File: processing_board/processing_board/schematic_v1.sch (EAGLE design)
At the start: 64 parts, among them J5 FEMALE 2x3, Q1 BSS138, Q2 BSS138, Q3 BSS138, Q4 BSS138

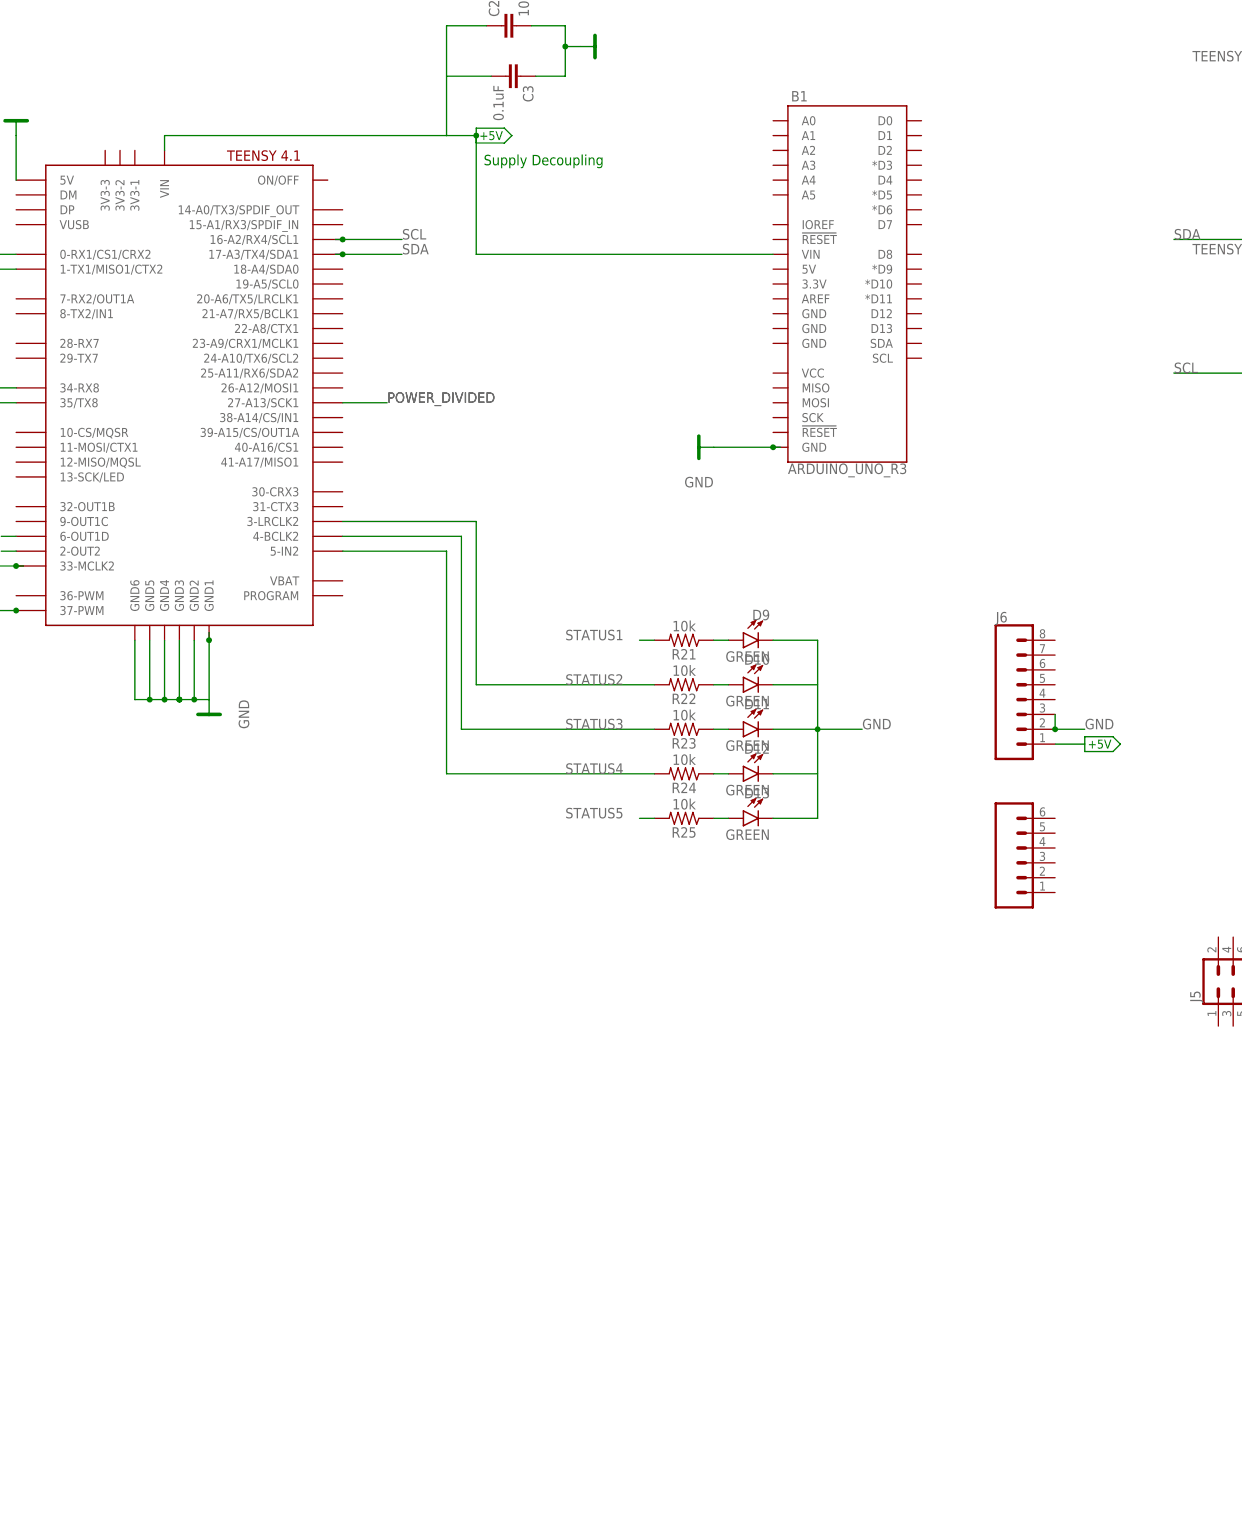
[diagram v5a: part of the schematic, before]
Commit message: added dip switch
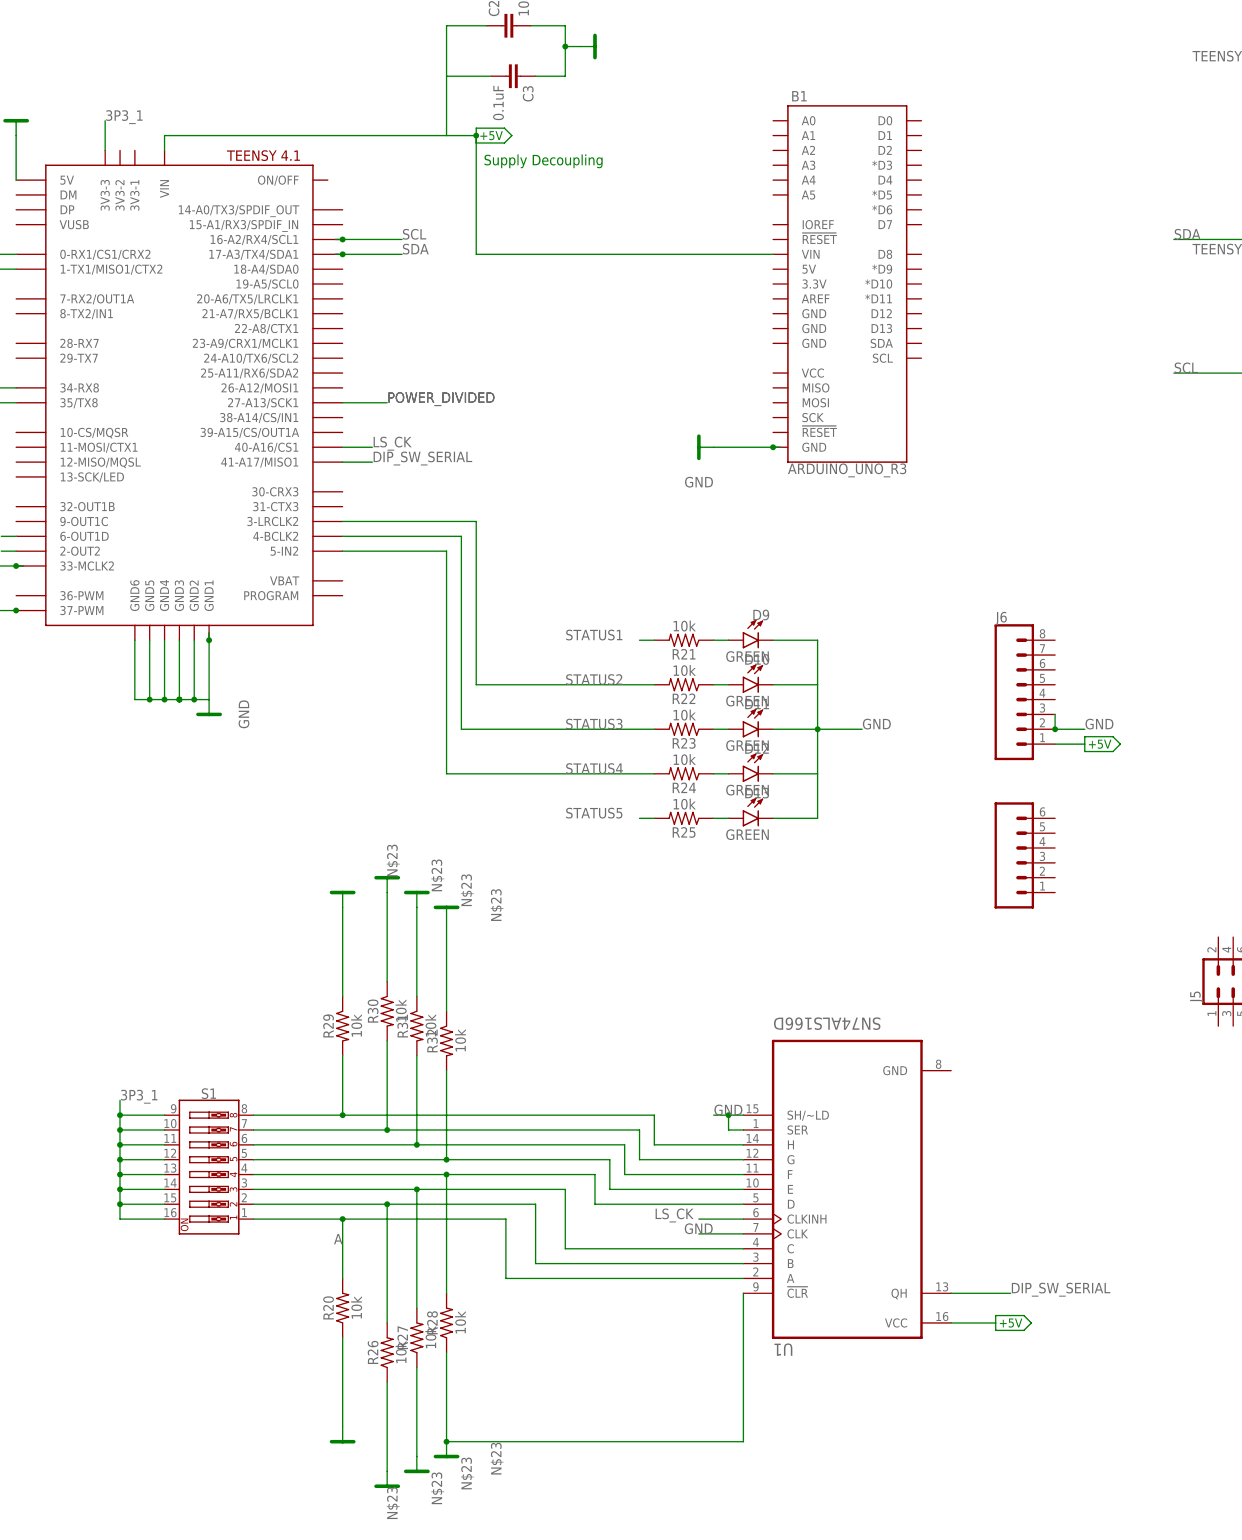
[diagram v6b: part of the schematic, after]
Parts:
- added R20, R26, R27, R28, R29, R30, R31, R32: 10k, SparkFun-Resistors:10KOHM-0603-1/10W-1%
- added S1: (no value), SparkFun-Switches:DIP-08-PTH
- added U1: SN74ALS166D, SN74ALS166D - TI level shifter:SN74ALS166D
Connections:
- new net 3P3_1: S1.10, S1.11, S1.12, S1.13, S1.14, S1.15, S1.16, S1.9, U$4.3V3-3
- new net A: R20.2, S1.1, U1.A
- new net C: R27.2, S1.3, U1.C
- new net D: R28.2, S1.4, U1.D
- new net DIP_SW_SERIAL: U$4.41-A17/MISO1, U1.QH
- new net E: R32.2, S1.5, U1.E
- new net H: R29.2, S1.8, U1.H
- new net LS_CK: U$4.40-A16/CS1, U1.CLKINH
- new net N$23: R20.1, R26.1, R27.1, R28.1, R29.1, R30.1, R31.1, R32.1, U1.!CLR
- new net N$25: R31.2, S1.6, U1.F
- new net N$30: R26.2, S1.2, U1.B
- new net N$9: R30.2, S1.7, U1.G
- net +5V: now also U1.VCC
- net GND: now also U1.CLK, U1.SER, U1.SH/~LD

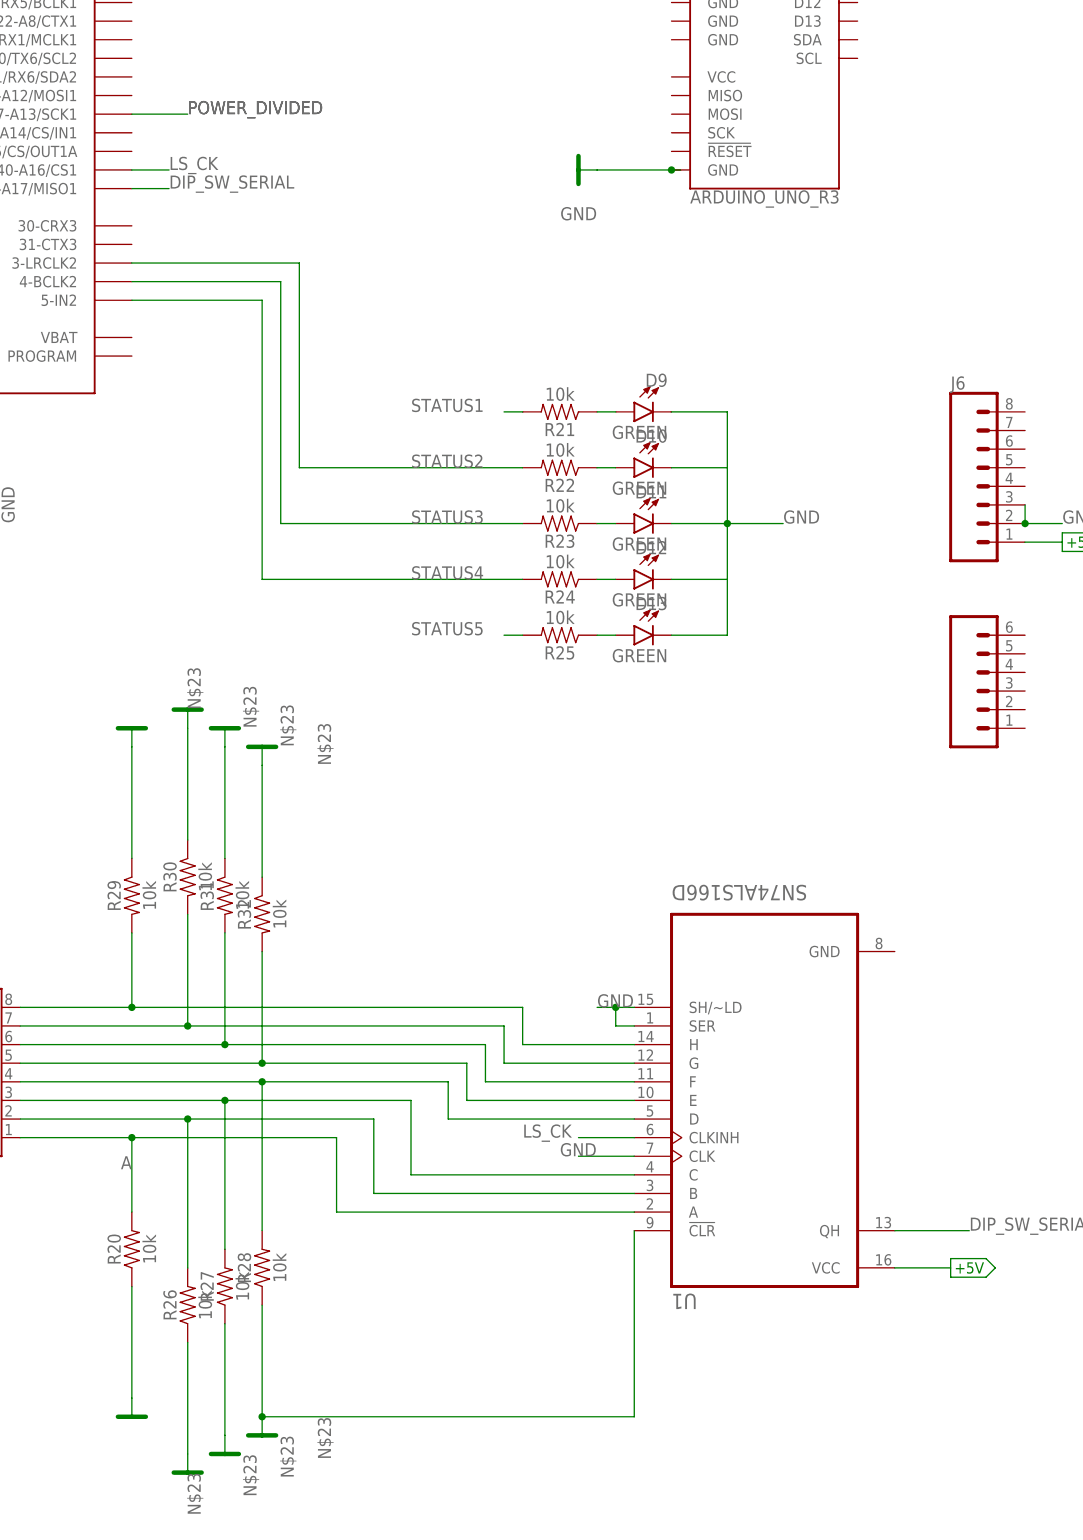
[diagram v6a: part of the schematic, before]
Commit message: fixed dip sw
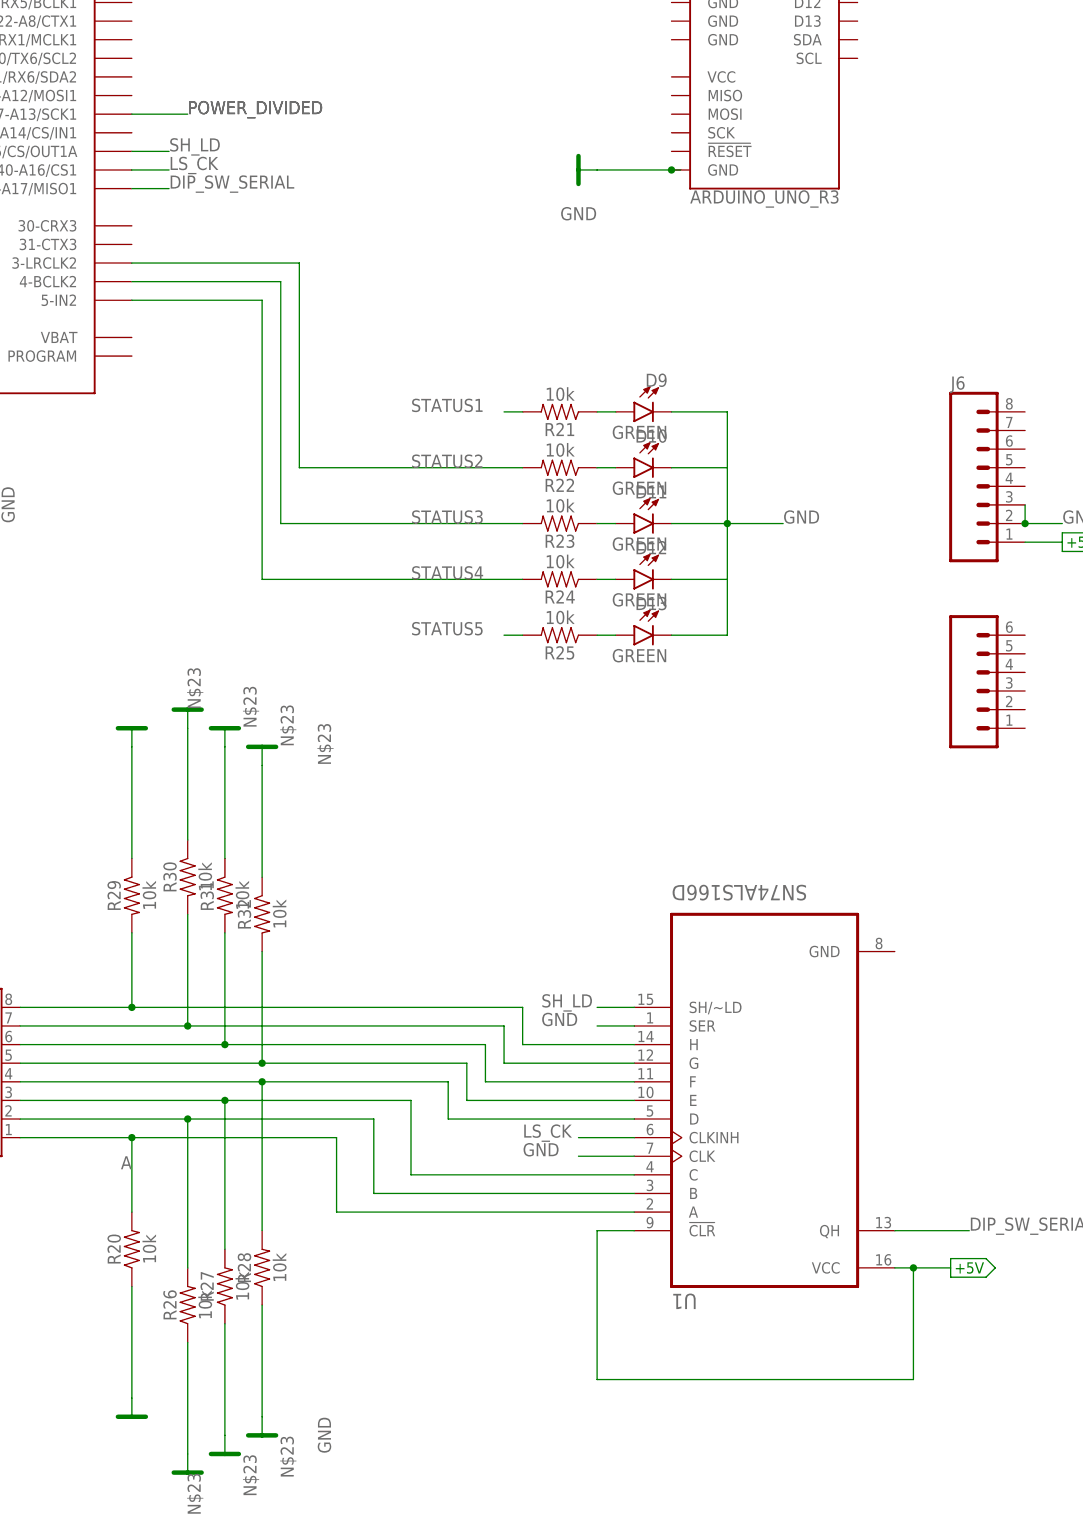
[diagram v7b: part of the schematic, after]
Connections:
- new net SH_LD: U$4.39-A15/CS/OUT1A, U1.SH/~LD
- net +5V: now also U1.!CLR
- net GND: now also R28.1; no longer U1.SH/~LD
- net N$23: no longer R28.1, U1.!CLR
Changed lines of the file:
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@@
 </segment>
 <segment>
-<pinref part="U1" gate="A" pin="SH/~LD"/>
-<wire x1="124.46" y1="-83.82" x2="121.92" y2="-83.82" width="0.1524" layer="91"/>
-<label x="119.38" y="-83.82" size="1.778" layer="95"/>
+<wire x1="124.46" y1="-86.36" x2="119.38" y2="-86.36" width="0.1524" layer="91"/>
 <pinref part="U1" gate="A" pin="SER"/>
-<wire x1="121.92" y1="-83.82" x2="119.38" y2="-83.82" width="0.1524" layer="91"/>
-<wire x1="124.46" y1="-86.36" x2="121.92" y2="-86.36" width="0.1524" layer="91"/>
-<wire x1="121.92" y1="-86.36" x2="121.92" y2="-83.82" width="0.1524" layer="91"/>
-<junction x="121.92" y="-83.82"/>
+<label x="111.76" y="-86.36" size="1.778" layer="95"/>
+</segment>
+<segment>
+<pinref part="R28" gate="G$1" pin="1"/>
+<pinref part="GND20" gate="VR1" pin="GND"/>
+<wire x1="73.66" y1="-139.7" x2="73.66" y2="-124.46" width="0.1524" layer="91"/>
+<label x="81.28" y="-139.7" size="1.778" layer="95" rot="R270"/>
 </segment>
 <segment>
 <pinref part="U1" gate="A" pin="CLK"/>
 <wire x1="124.46" y1="-104.14" x2="116.84" y2="-104.14" width="0.1524" layer="91"/>
-<label x="114.3" y="-104.14" size="1.778" layer="95"/>
+<label x="109.22" y="-104.14" size="1.778" layer="95"/>
 </segment>
 </net>
@@
 <segment>
 <pinref part="U1" gate="A" pin="VCC"/>
-<wire x1="160.02" y1="-119.38" x2="167.64" y2="-119.38" width="0.1524" layer="91"/>
+<wire x1="160.02" y1="-119.38" x2="162.56" y2="-119.38" width="0.1524" layer="91"/>
 <pinref part="PWR18" gate="G$1" pin="+5V"/>
+<pinref part="U1" gate="A" pin="!CLR"/>
+<wire x1="162.56" y1="-119.38" x2="167.64" y2="-119.38" width="0.1524" layer="91"/>
+<wire x1="124.46" y1="-114.3" x2="119.38" y2="-114.3" width="0.1524" layer="91"/>
+<wire x1="119.38" y1="-114.3" x2="119.38" y2="-134.62" width="0.1524" layer="91"/>
+<wire x1="119.38" y1="-134.62" x2="162.56" y2="-134.62" width="0.1524" layer="91"/>
+<wire x1="162.56" y1="-134.62" x2="162.56" y2="-119.38" width="0.1524" layer="91"/>
+<junction x="162.56" y="-119.38"/>
 </segment>
 </net>
@@
 <label x="76.2" y="-142.24" size="1.778" layer="95" rot="R270"/>
 <wire x1="68.58" y1="-142.24" x2="68.58" y2="-127" width="0.1524" layer="91"/>
-</segment>
-<segment>
-<pinref part="R28" gate="G$1" pin="1"/>
-<pinref part="GND20" gate="VR1" pin="GND"/>
-<label x="81.28" y="-139.7" size="1.778" layer="95" rot="R270"/>
-<wire x1="73.66" y1="-139.7" x2="73.66" y2="-124.46" width="0.1524" layer="91"/>
-<pinref part="U1" gate="A" pin="!CLR"/>
-<wire x1="124.46" y1="-114.3" x2="124.46" y2="-139.7" width="0.1524" layer="91"/>
-<wire x1="124.46" y1="-139.7" x2="73.66" y2="-139.7" width="0.1524" layer="91"/>
-<junction x="73.66" y="-139.7"/>
 </segment>
 <segment>
@@
 </segment>
 </net>
+<net name="SH_LD" class="0">
+<segment>
+<pinref part="U1" gate="A" pin="SH/~LD"/>
+<label x="111.76" y="-83.82" size="1.778" layer="95"/>
+<wire x1="124.46" y1="-83.82" x2="119.38" y2="-83.82" width="0.1524" layer="91"/>
+</segment>
+<segment>
+<pinref part="U$4" gate="G$1" pin="39-A15/CS/OUT1A"/>
+<wire x1="55.88" y1="33.02" x2="60.96" y2="33.02" width="0.1524" layer="91"/>
+<label x="60.96" y="33.02" size="1.778" layer="95"/>
+</segment>
+</net>

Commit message: updated board
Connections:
- removed net 3P3_1: S1.10, S1.11, S1.12, S1.13, S1.14, S1.15, S1.16, S1.9, U$4.3V3-3
- new net N$19: B1.GND
- net +5V: no longer B1.VIN, U1.!CLR, U1.VCC
- net GND: now also U1.GND; no longer B1.GND
- net TEENSY_3.3V: now also S1.10, S1.11, S1.12, S1.13, S1.14, S1.15, S1.16, S1.9, U$4.3V3-1, U$4.3V3-2, U$4.3V3-3, U1.!CLR, U1.VCC
